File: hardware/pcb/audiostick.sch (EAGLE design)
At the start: 64 parts, among them IC1 TPS73633MBDV, IC3 PCM5102ASW, IC5 AP22804W5, IC6 TINY13V-10SSU, J1 AVRISP6TH127, J2 AUDIO_JACK_3.5MM_PTH, J3 USB-B

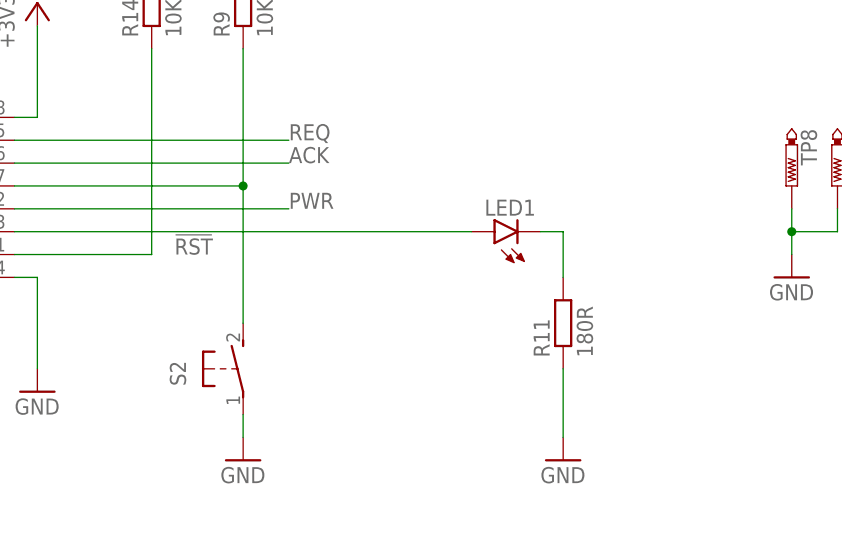
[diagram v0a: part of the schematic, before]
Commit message: Complete revision of design - layout, connections, parts. Ready for proto run
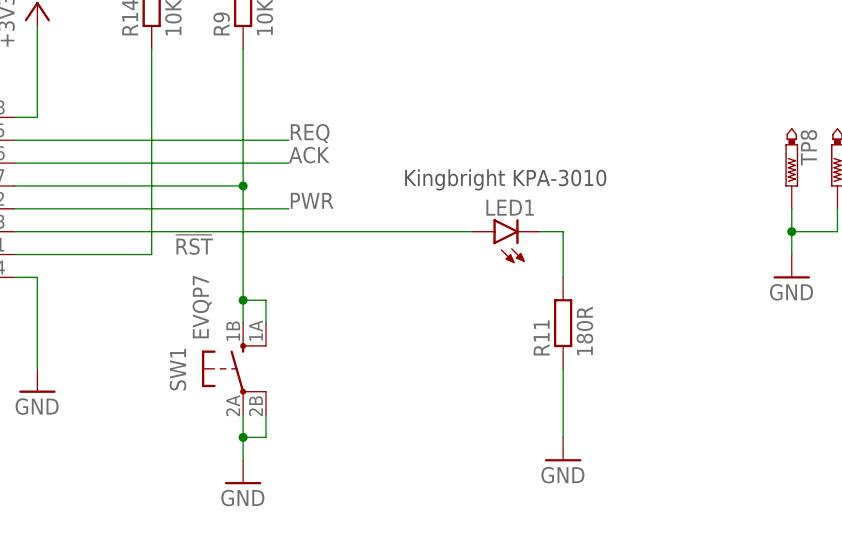
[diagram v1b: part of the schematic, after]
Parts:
- removed S2: (no value), switch-omron:31-XX
- added SW1: EVQP7, AudioStick:EVQP7
- LED1: value (none) -> LEDLED; device led:LED3MM -> AudioStick:LEDLED
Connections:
- net GND: now also SW1.P, SW1.P1; no longer S2.P
- net SW: now also SW1.S, SW1.S1; no longer S2.S
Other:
- note added: "Kingbright KPA-3010"
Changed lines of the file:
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@@
 <part name="P+1" library="supply1" library_urn="urn:adsk.eagle:library:371" deviceset="V+" device=""/>
 <part name="GND3" library="supply1" library_urn="urn:adsk.eagle:library:371" deviceset="GND" device=""/>
-<part name="S2" library="switch-omron" library_urn="urn:adsk.eagle:library:377" deviceset="31-XX" device="" package3d_urn="urn:adsk.eagle:package:27487/1"/>
 <part name="IC3" library="AudioStick" deviceset="PCM5102A" device="SW" package3d_urn="urn:adsk.eagle:package:4349/2"/>
 <part name="FRAME2" library="frames" library_urn="urn:adsk.eagle:library:229" deviceset="A3P-LOC" device=""/>
@@
 <part name="R13" library="rcl" library_urn="urn:adsk.eagle:library:334" deviceset="R-EU_" device="R0603" package3d_urn="urn:adsk.eagle:package:23555/3" value="10K"/>
 <part name="IC6" library="atmel" library_urn="urn:adsk.eagle:library:105" deviceset="TINY13" device="SSU" package3d_urn="urn:adsk.eagle:package:4358/1" technology="V-10"/>
-<part name="LED1" library="led" library_urn="urn:adsk.eagle:library:259" deviceset="LED" device="3MM" package3d_urn="urn:adsk.eagle:package:15797/1"/>
 <part name="J1" library="AWJLEagleLib" deviceset="AVRISP6" device="TH127"/>
 <part name="+3V5" library="supply1" library_urn="urn:adsk.eagle:library:371" deviceset="+3V3" device=""/>
@@
 <part name="C16" library="rcl" library_urn="urn:adsk.eagle:library:334" deviceset="C-EU" device="C0603" package3d_urn="urn:adsk.eagle:package:23616/2" value="10n"/>
 <part name="GND33" library="supply1" library_urn="urn:adsk.eagle:library:371" deviceset="GND" device=""/>
+<part name="SW1" library="AudioStick" deviceset="EVQP7" device=""/>
+<part name="LED1" library="AudioStick" deviceset="LED" device="LED"/>
 </parts>
 <sheets>
@@
 pull down at boot</text>
 <text x="121.92" y="114.3" size="1.778" layer="97">ATtiny13 supply</text>
+<text x="96.52" y="43.18" size="1.778" layer="97">Kingbright KPA-3010</text>
 </plain>
 <instances>
@@
 <attribute name="VALUE" x="53.34" y="17.78" size="1.778" layer="96"/>
 </instance>
-<instance part="S2" gate="1" x="78.74" y="22.86" smashed="yes">
-<attribute name="NAME" x="72.39" y="20.955" size="1.778" layer="95" rot="R90"/>
-<attribute name="VALUE" x="74.93" y="26.035" size="1.778" layer="96" rot="R90"/>
-</instance>
 <instance part="IC3" gate="G$1" x="63.5" y="246.38" smashed="yes">
 <attribute name="NAME" x="48.26" y="271.78" size="1.778" layer="95"/>
@@
 <attribute name="VALUE" x="76.2" y="68.58" size="1.778" layer="96" rot="R90"/>
 </instance>
-<instance part="GND1" gate="1" x="78.74" y="12.7" smashed="yes">
-<attribute name="VALUE" x="76.2" y="10.16" size="1.778" layer="96"/>
+<instance part="GND1" gate="1" x="78.74" y="10.16" smashed="yes">
+<attribute name="VALUE" x="76.2" y="7.62" size="1.778" layer="96"/>
 </instance>
 <instance part="R9" gate="G$1" x="78.74" y="63.5" smashed="yes" rot="R90">
@@
 <attribute name="VALUE" x="50.8" y="27.94" size="1.778" layer="96" rot="MR0"/>
 </instance>
-<instance part="LED1" gate="G$1" x="106.68" y="38.1" smashed="yes" rot="R90">
-<attribute name="NAME" x="111.252" y="41.656" size="1.778" layer="95" rot="R180"/>
-<attribute name="VALUE" x="111.252" y="43.815" size="1.778" layer="96" rot="R180"/>
-</instance>
 <instance part="J1" gate="G$1" x="220.98" y="40.64" smashed="yes">
 <attribute name="NAME" x="213.36" y="33.02" size="1.778" layer="95"/>
@@
 <instance part="GND33" gate="1" x="58.42" y="86.36" smashed="yes">
 <attribute name="VALUE" x="55.88" y="83.82" size="1.778" layer="96"/>
+</instance>
+<instance part="SW1" gate="G$1" x="78.74" y="22.86" smashed="yes">
+<attribute name="NAME" x="72.39" y="20.32" size="1.778" layer="95" rot="R90"/>
+<attribute name="VALUE" x="74.93" y="26.035" size="1.778" layer="96" rot="R90"/>
+</instance>
+<instance part="LED1" gate="G$1" x="106.68" y="38.1" smashed="yes" rot="R90">
+<attribute name="NAME" x="111.252" y="41.656" size="1.778" layer="95" rot="R180"/>
 </instance>
 </instances>
@@
 <segment>
 <pinref part="GND1" gate="1" pin="GND"/>
-<pinref part="S2" gate="1" pin="P"/>
+<wire x1="78.74" y1="12.7" x2="78.74" y2="15.24" width="0.1524" layer="91"/>
+<pinref part="SW1" gate="G$1" pin="P"/>
+<pinref part="SW1" gate="G$1" pin="P1"/>
 <wire x1="78.74" y1="15.24" x2="78.74" y2="17.78" width="0.1524" layer="91"/>
+<wire x1="78.74" y1="15.24" x2="81.28" y2="15.24" width="0.1524" layer="91"/>
+<wire x1="81.28" y1="15.24" x2="81.28" y2="17.78" width="0.1524" layer="91"/>
+<junction x="78.74" y="15.24"/>
 </segment>
 <segment>
@@
 <net name="SW" class="0">
 <segment>
-<pinref part="S2" gate="1" pin="S"/>
 <pinref part="R9" gate="G$1" pin="1"/>
-<wire x1="78.74" y1="27.94" x2="78.74" y2="43.18" width="0.1524" layer="91"/>
+<wire x1="78.74" y1="27.94" x2="78.74" y2="30.48" width="0.1524" layer="91"/>
 <pinref part="IC6" gate="G$1" pin="PB2/PCINT2/SCK/ADC1/T0"/>
+<wire x1="78.74" y1="30.48" x2="78.74" y2="43.18" width="0.1524" layer="91"/>
 <wire x1="78.74" y1="43.18" x2="78.74" y2="58.42" width="0.1524" layer="91"/>
 <wire x1="53.34" y1="43.18" x2="78.74" y2="43.18" width="0.1524" layer="91"/>
 <junction x="78.74" y="43.18"/>
+<pinref part="SW1" gate="G$1" pin="S"/>
+<pinref part="SW1" gate="G$1" pin="S1"/>
+<wire x1="78.74" y1="30.48" x2="81.28" y2="30.48" width="0.1524" layer="91"/>
+<wire x1="81.28" y1="30.48" x2="81.28" y2="27.94" width="0.1524" layer="91"/>
+<junction x="78.74" y="30.48"/>
 </segment>
 <segment>
@@
 <segment>
 <pinref part="IC6" gate="G$1" pin="PB4/PCINT4/ADC2"/>
+<wire x1="53.34" y1="38.1" x2="104.14" y2="38.1" width="0.1524" layer="91"/>
 <pinref part="LED1" gate="G$1" pin="A"/>
-<wire x1="53.34" y1="38.1" x2="104.14" y2="38.1" width="0.1524" layer="91"/>
 </segment>
 </net>
 <net name="N$15" class="0">
 <segment>
-<pinref part="LED1" gate="G$1" pin="C"/>
 <wire x1="111.76" y1="38.1" x2="114.3" y2="38.1" width="0.1524" layer="91"/>
 <pinref part="R11" gate="G$1" pin="2"/>
 <wire x1="114.3" y1="38.1" x2="114.3" y2="33.02" width="0.1524" layer="91"/>
-</segment>
-</net>
+<pinref part="LED1" gate="G$1" pin="C"/>
+</segment>
+</net>

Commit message: Final revision before manufacture
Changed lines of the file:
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@@
 <instance part="Q2" gate="N" x="215.9" y="91.44" smashed="yes">
 <attribute name="VALUE" x="204.47" y="91.44" size="1.778" layer="96"/>
-<attribute name="NAME" x="204.47" y="93.98" size="1.778" layer="95"/>
+<attribute name="NAME" x="219.71" y="86.36" size="1.778" layer="95"/>
 </instance>
 <instance part="Q2" gate="P" x="220.98" y="104.14" smashed="yes" rot="R90">
 <attribute name="VALUE" x="224.79" y="92.71" size="1.778" layer="96" rot="R90"/>
-<attribute name="NAME" x="222.25" y="92.71" size="1.778" layer="95" rot="R90"/>
+<attribute name="NAME" x="224.79" y="102.87" size="1.778" layer="95" rot="R180"/>
 </instance>
 <instance part="GND20" gate="1" x="22.86" y="86.36" smashed="yes">
@@
 <wire x1="81.28" y1="30.48" x2="81.28" y2="27.94" width="0.1524" layer="91"/>
 <junction x="78.74" y="30.48"/>
-</segment>
-<segment>
+<label x="83.82" y="43.18" size="1.778" layer="95"/>
+</segment>
+<segment>

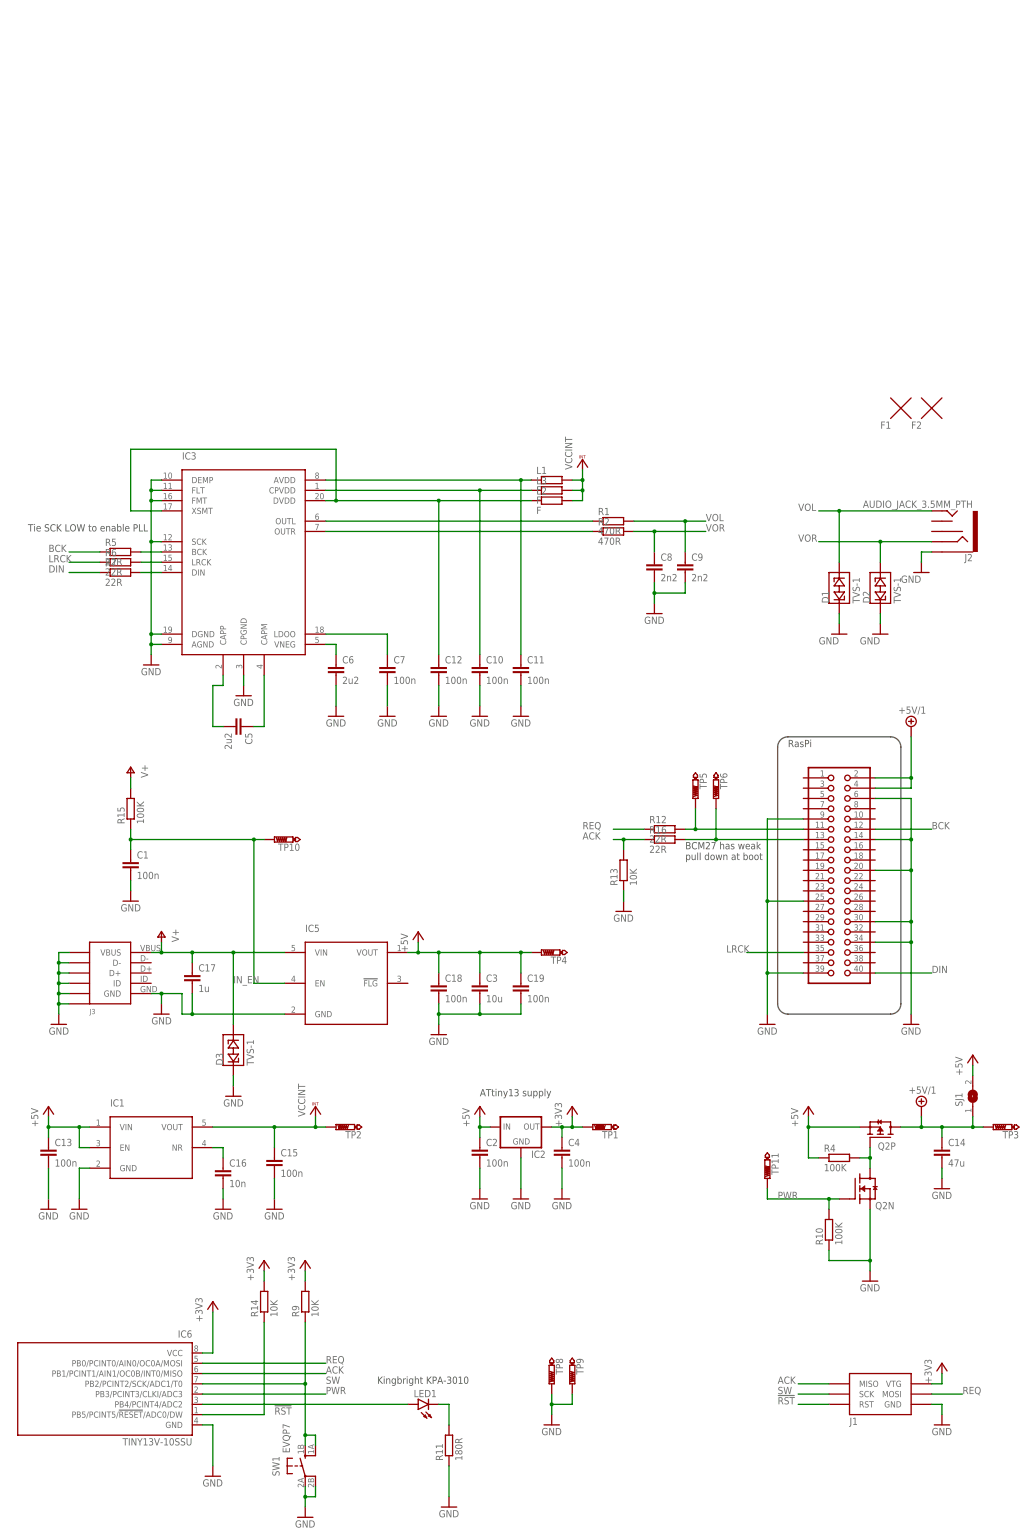
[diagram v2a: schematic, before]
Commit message: 2.0 -> 2.1 simplification, PCB rearrangement
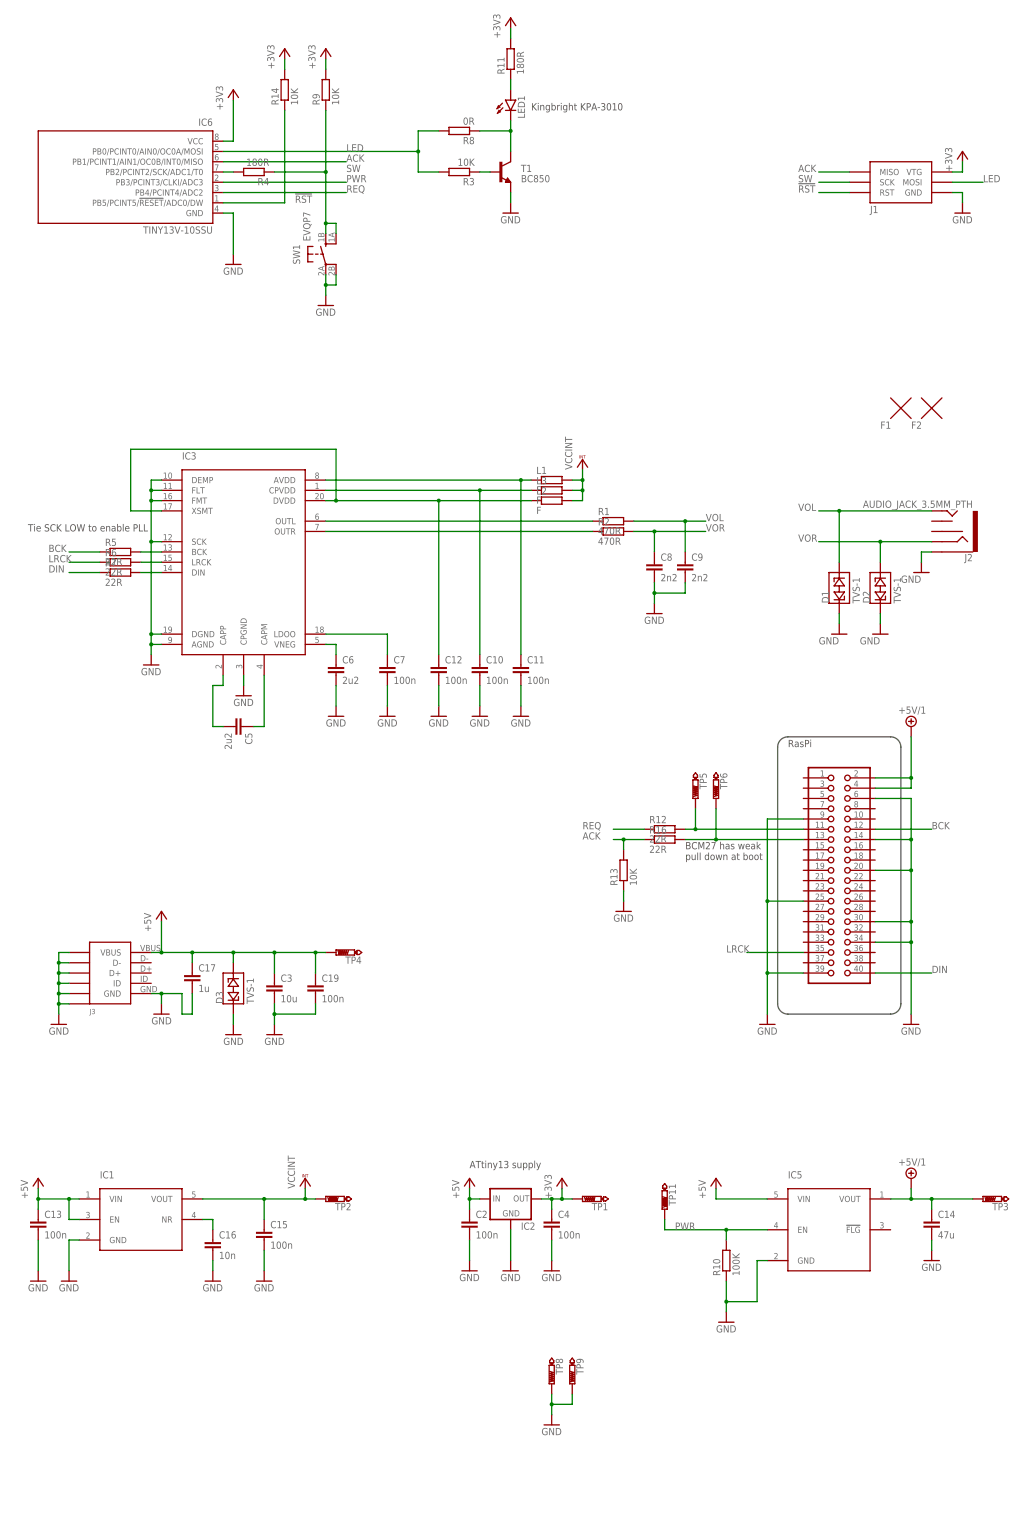
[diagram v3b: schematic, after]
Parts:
- removed C1, C18: 100n, rcl:C-EUC0603
- removed Q2: (no value), AWJLEagleLib:BSL215
- removed R15: 100K, rcl:R-EU_R0603
- removed SJ1: (no value), jumper:SJ
- removed TP10: PTR1PAD1-13, testpad:PTR1PAD1-13
- added R3: 10K, rcl:R-EU_R0603
- added R8: 0R, rcl:R-EU_R0603
- added T1: BC850, transistor:BC850
- R4: value 100K -> 180R
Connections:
- removed net IN_EN: C1.1, IC5.EN, R15.1, TP10.TP
- removed net V+: C17.1, D3.3, IC5.VIN, J3.VBUS, R15.2
- new net N$17: LED1.A, R11.1
- new net N$18: IC6.PB2/PCINT2/SCK/ADC1/T0, R4.2
- net +3V3: now also R11.2
- net +5V: now also C17.1, D3.3, IC5.VIN, J3.VBUS; no longer C18.1, IC5.VOUT, Q2P.S, R4.1, SJ1.2
- net +5V/1: now also IC5.VOUT; no longer Q2P.D, SJ1.1
- net GND: now also T1.E; no longer C1.2, C18.2, Q2N.S, R11.1
- net LED: now also IC6.PB0/PCINT0/AIN0/OC0A/MOSI, J1.MOSI, R3.2, R8.2; no longer IC6.PB4/PCINT4/ADC2, LED1.A
- net N$15: now also R8.1, T1.C; no longer R11.2
- net N$6: now also R3.1, T1.B; no longer Q2N.D, Q2P.G, R4.2
- net PWR: now also IC5.EN; no longer Q2N.G
- net REQ: now also IC6.PB4/PCINT4/ADC2; no longer IC6.PB0/PCINT0/AIN0/OC0A/MOSI, J1.MOSI
- net SW: now also R4.1; no longer IC6.PB2/PCINT2/SCK/ADC1/T0
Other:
- moved on the sheet: C13, C14, C15, C16, C19, C2, C3, C4, D3, IC1, IC2, IC5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

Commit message: Change switch
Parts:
- removed SW1: EVQP7, AudioStick:EVQP7
- added S1: (no value), switch-omron:31-XX
- C14: value 47u -> 2u2; device rcl:C-EUC1206 -> rcl:C-EUC0805
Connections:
- net GND: now also S1.P; no longer SW1.P, SW1.P1
- net SW: now also S1.S; no longer SW1.S, SW1.S1
